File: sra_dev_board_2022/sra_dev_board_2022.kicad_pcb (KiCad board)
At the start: 2 copper layers, 81.2 x 92.7 mm, 183 parts, among them J1 Conn_01x19_Male, J10 Conn_01x03_Male, J11 Conn_01x05_Male, J12 Conn_01x05_Male, J13 Conn_01x05_Male, J2 Conn_01x03_Male, J3 Conn_01x03_Male, J4 Conn_01x03_Male, J5 Conn_01x19_Male, J6 DCJ200-10-A-XX-X_REVA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

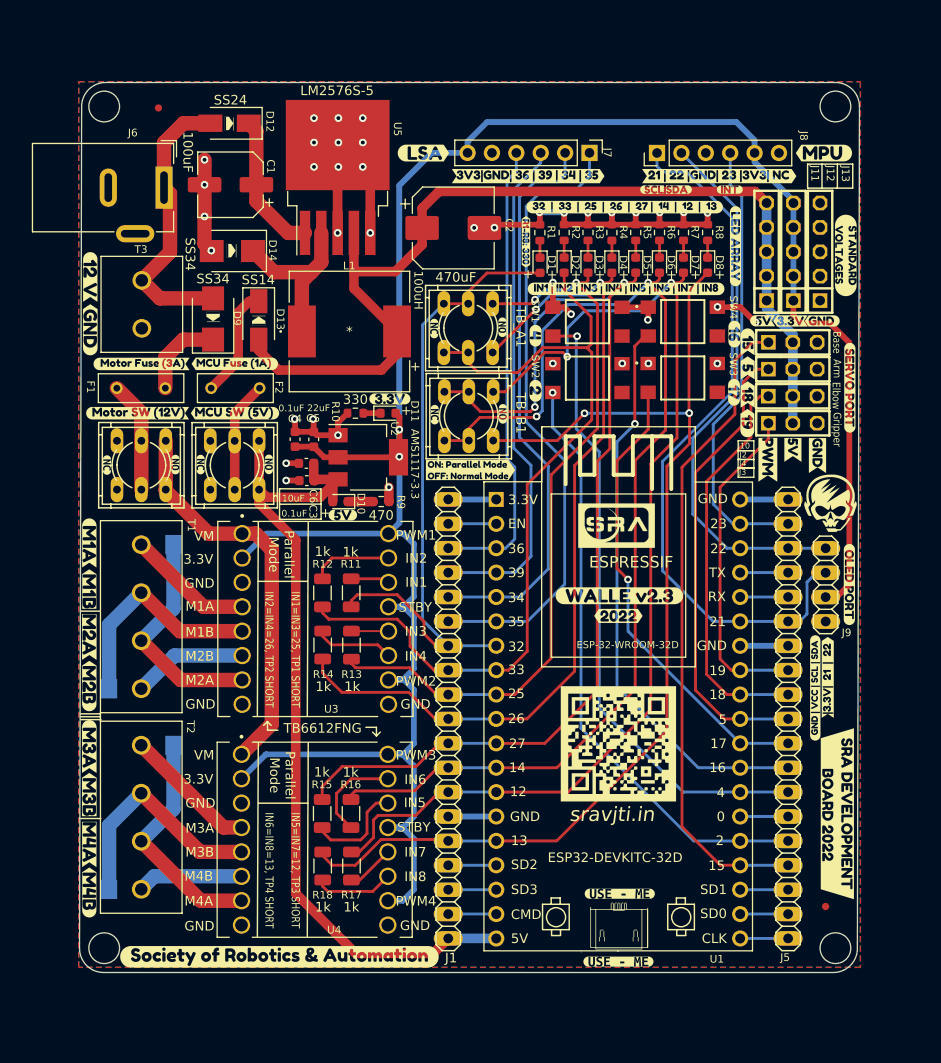
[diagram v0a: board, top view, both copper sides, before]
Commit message: Added drv8825 stepper motor driver
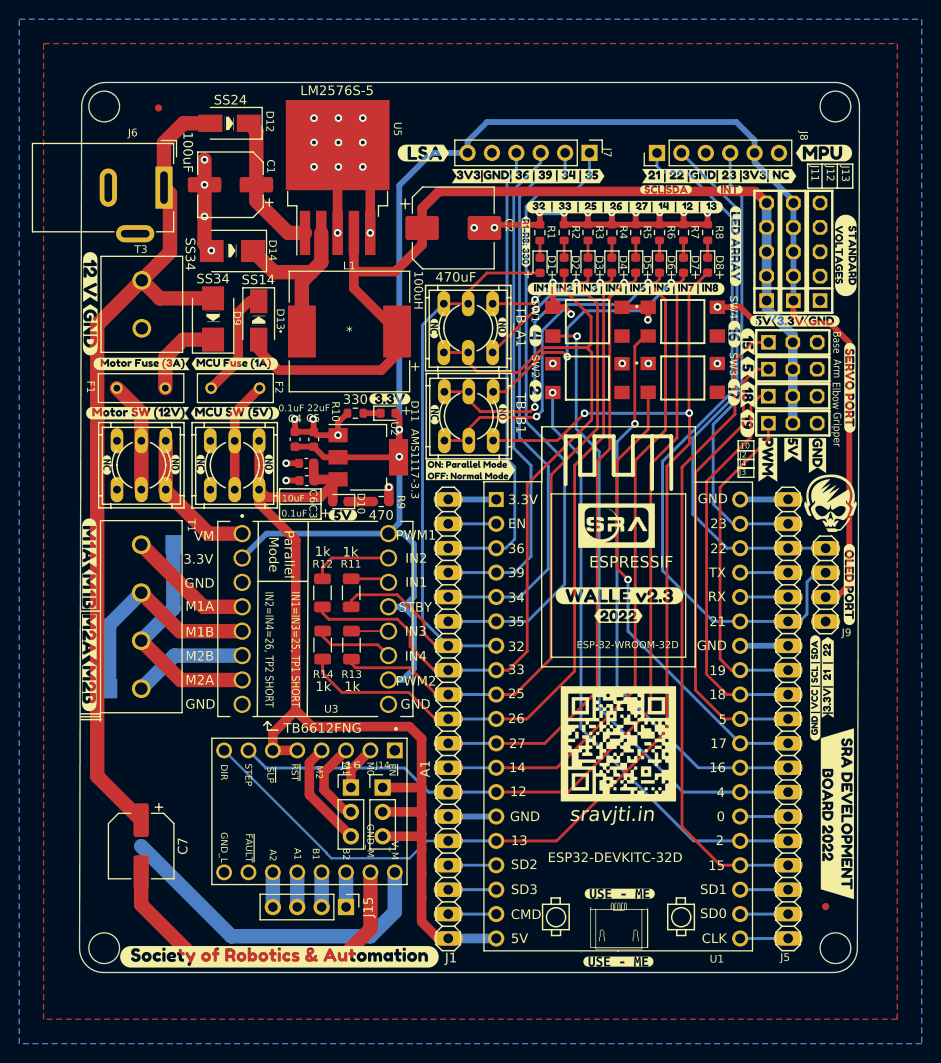
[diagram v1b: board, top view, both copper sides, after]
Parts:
- removed R15, R16, R17, R18: 1k, Resistor_SMD:R_1206_3216Metric
- removed T2: Screw_Terminal_01x04, terminal_block:motor_1x04_tht
- removed TP3, TP4: TestPoint, testpoint_pad:pad_1,27-2,54_smd
- removed U4: TB6612FNG, motor_driver:TB6612FNG_2
- removed kibuzzard-61F712DA: G***, kibuzzard-61F712DA
- removed kibuzzard-61F712EB: G***, kibuzzard-61F712EB
- removed kibuzzard-61F71302: G***, kibuzzard-61F71302
- removed kibuzzard-61F71318: G***, kibuzzard-61F71318
- added A1: drv8825, motor_driver:IC_DRV8825_STEPPER_MOTOR_DRIVER_CARRIER, F.Cu at (93.7, 105.4)
- added C7: 100uF, Capacitor_SMD:CP_Elec_6.3x7.7, F.Cu at (76.2, 109.0)
- added J14: Conn_01x03_Male, Connector_PinHeader_2.54mm:PinHeader_1x03_P2.54mm_Vertical, F.Cu at (101.3, 102.9)
- added J15: Conn_01x04_Male, Connector_PinHeader_2.54mm:PinHeader_1x04_P2.54mm_Vertical, F.Cu at (97.5, 115.3)
- added J16: Conn_01x03_Male, Connector_PinHeader_2.54mm:PinHeader_1x03_P2.54mm_Vertical, F.Cu at (98.0, 102.9)
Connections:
- R11 pad 2: Net-(R11-Pad2) -> unconnected-(R11-Pad2)
- R12 pad 2: Net-(R12-Pad2) -> unconnected-(R12-Pad2)
- R13 pad 2: Net-(R13-Pad2) -> unconnected-(R13-Pad2)
- R14 pad 2: Net-(R14-Pad2) -> unconnected-(R14-Pad2)
- TB_B1 pad 2: /27 -> /BIN1
- TB_B1 pad 5: /14 -> /BIN2
- U3 pad 10: /3V3 -> unconnected-(U3-Pad10)
- U3 pad 11: Net-(R14-Pad2) -> unconnected-(U3-Pad11)
- U3 pad 12: Net-(R13-Pad2) -> unconnected-(U3-Pad12)
- U3 pad 13: /3V3 -> unconnected-(U3-Pad13)
- U3 pad 14: Net-(R11-Pad2) -> unconnected-(U3-Pad14)
- U3 pad 15: Net-(R12-Pad2) -> unconnected-(U3-Pad15)
- U3 pad 16: /3V3 -> unconnected-(U3-Pad16)
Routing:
- net /12V_U: track 29.7 -> 125.2 mm
- net /3V3: track 240.1 -> 190.2 mm
- net GND: track 105.9 -> 142.4 mm
- net /12V_P: track 41.4 -> 15.0 mm
- net /OUT3B: track 24.4 -> 3.61 mm
- net /OUT2B: track 24.4 -> 3.61 mm
- net /5V_P: track 89.0 -> 107.9 mm
- net /27: track 110.7 -> 95.3 mm
- net /13: track 113.6 -> 127.5 mm
- net /M2: track 0.00 -> 11.3 mm
- net /14: track 114.7 -> 104.0 mm
- net Net-(R15-Pad2): track 10.5 -> 0.00 mm
- net /OUT1B: track 14.0 -> 3.61 mm
- net Net-(R16-Pad2): track 10.2 -> 0.00 mm
- net /12: track 111.6 -> 121.5 mm
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- added copper zone on F.Cu, net GND
- removed copper zone on F.Cu, net (none)
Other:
- board text removed: "IN5"
- board text removed: "IN5=IN7=12, TP3 SHORT IN6=IN8=13, TP4 SHORT"
- board text removed: "IN6"
- board text removed: "IN7"
- board text removed: "IN8"
- board text removed: "M3B"
- board text removed: "M4B"
- board text removed: "PWM3"
- board text removed: "PWM4"
- board text removed: "TP3"
- board text removed: "TP4"
